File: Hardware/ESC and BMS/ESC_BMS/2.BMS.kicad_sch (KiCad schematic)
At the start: 39 parts, among them J301 SW IN, J302 SW OUT, Q301 SQJ141ELP, Q302 SQJ141ELP, Q303 FDV304P, Q304 PMV20XNEA, Q305 SQJ141ELP, U301 BQ2057W, U302 BQ2969

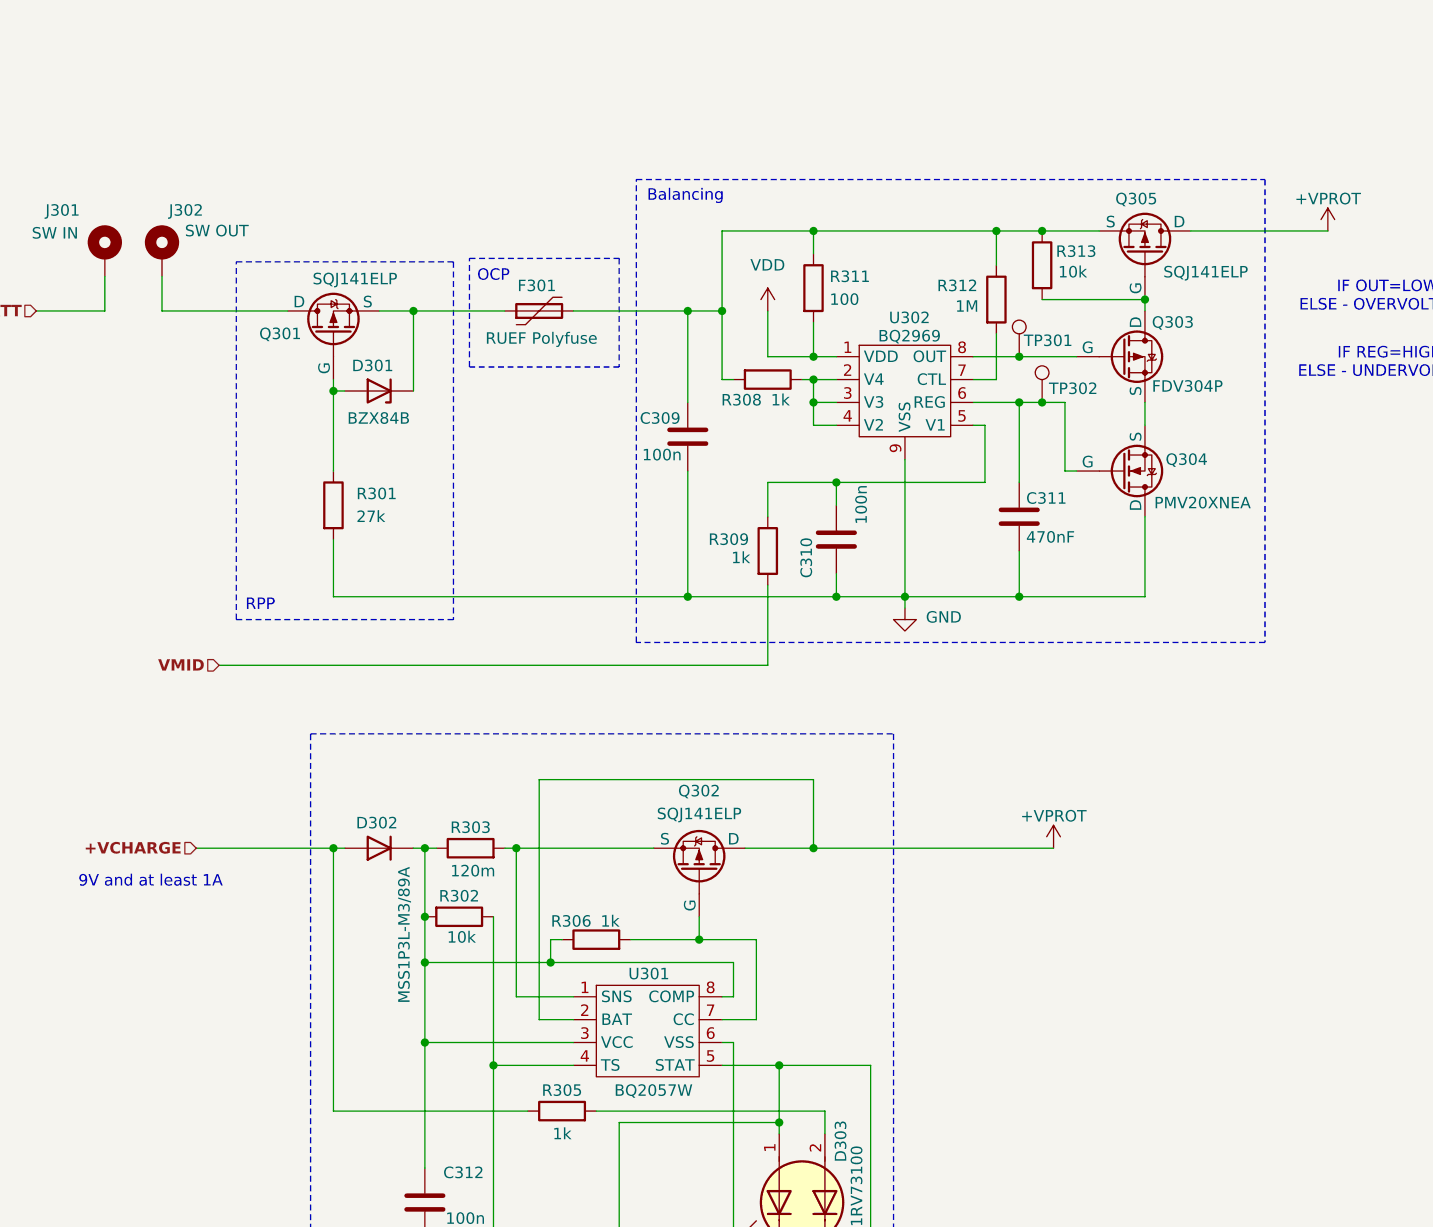
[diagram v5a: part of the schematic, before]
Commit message: Light rework of ESC/BMS layout
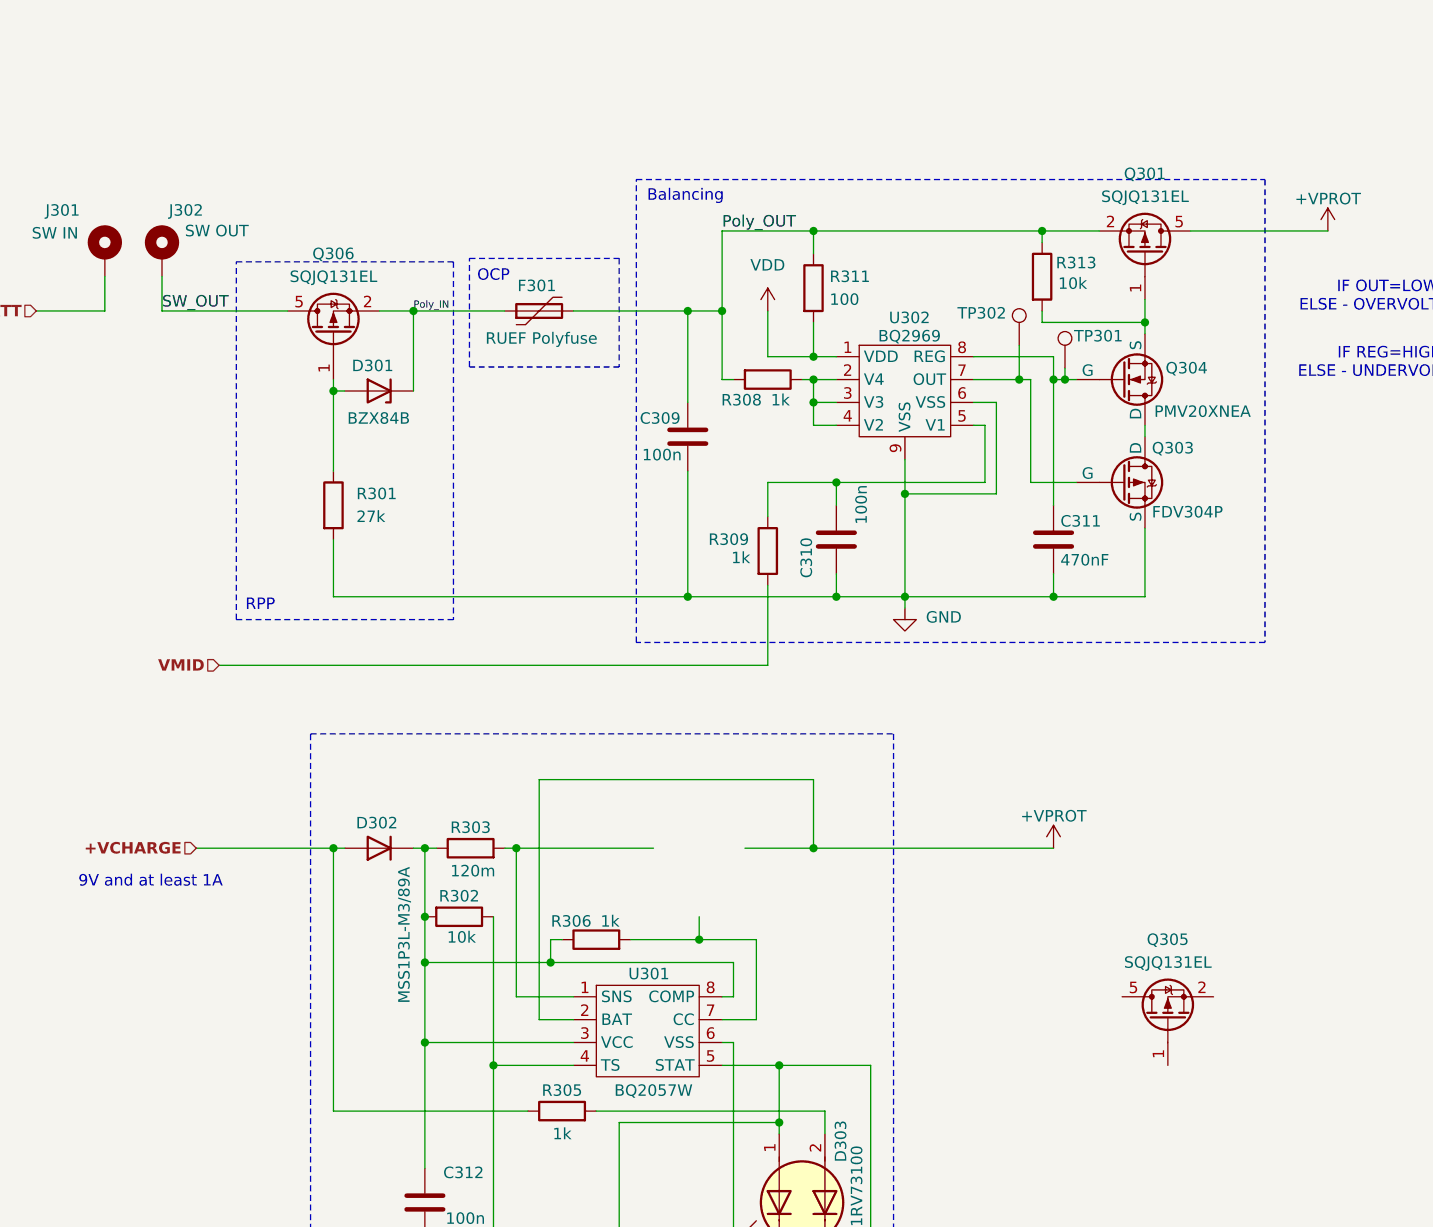
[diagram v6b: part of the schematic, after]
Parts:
- removed Q301, Q302, Q305: SQJ141ELP, Package_SO:PowerPAK_SO-8L_Single, symbol Simulation_SPICE:PMOS
- removed R312: 1M, Resistor_SMD:R_0805_2012Metric_Pad1.20x1.40mm_HandSolder, symbol Device:R
- added Q301, Q305, Q306: SQJQ131EL, Package_SO:PowerPAK_SO-8L_Single, symbol Transistor_FET:SQJQ131EL
- C302: footprint Capacitor_SMD:C_0805_2012Metric_Pad1.18x1.45mm_HandSolder -> Capacitor_SMD:C_0603_1608Metric_Pad1.08x0.95mm_HandSolder
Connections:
- net +VPROT: now also Q301.5 (D)
- net GND: now also Q303.3 (S), U302.6 (VSS); no longer Q304.1 (D)
- net at TP301.1, U302.8 (REG): now also C311.1, Q304.2 (G); no longer Q303.2 (G)
- net at R313.2: now also Q304.3 (S), Q301.1 (G); no longer Q303.1 (D)
- net Poly_OUT: now reaches C309.1, F301.2, R308.2, R311.1, R313.1
- net Poly_OUT: now also Q301.2 (S), Q301.3 (S), Q301.4 (S)
- net Poly_IN: now reaches D301.1 (K), F301.1
- net Poly_IN: now also Q306.2 (S), Q306.3 (S), Q306.4 (S)
- net at D301.2 (A), R301.1: now also Q306.1 (G)
- net SW_OUT: now reaches J302.1
- net SW_OUT: now also Q306.5 (D)
- net at U302.7 (OUT): now also Q303.2 (G), TP302.1
- new net: Q305.2 (S), Q305.3 (S), Q305.4 (S)
- new net: Q303.1 (D), Q304.1 (D)
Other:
- moved on the sheet: C311, Q303, Q304, R313, TP301, TP302

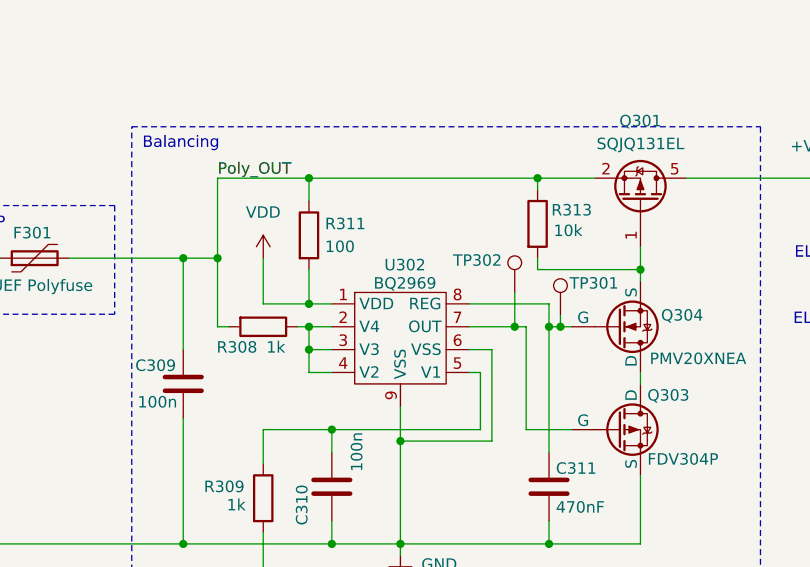
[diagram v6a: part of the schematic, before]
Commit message: ESC/BMS board done fully
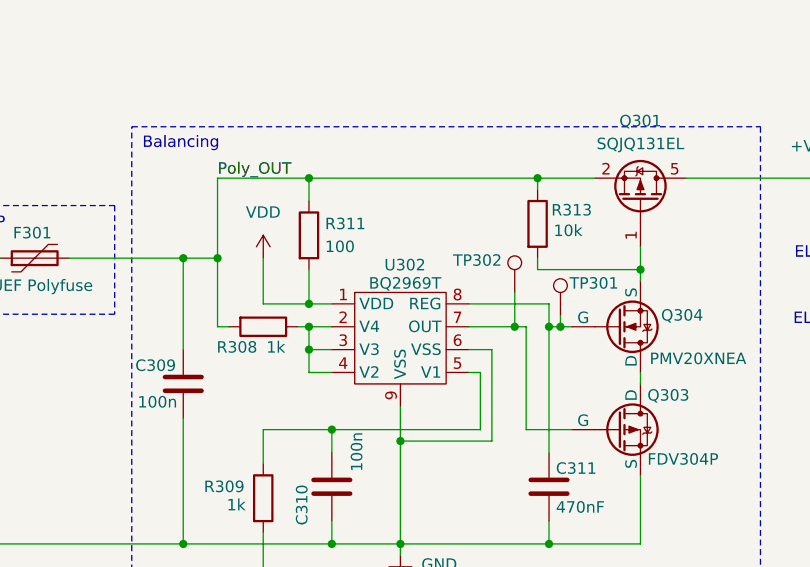
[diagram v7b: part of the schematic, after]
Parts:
- U302: value BQ2969 -> BQ2969T
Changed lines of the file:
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@@
 			)
 		)
-		(property "Value" "BQ2969"
+		(property "Value" "BQ2969T"
 			(at 226.568 98.044 0)
 			(effects

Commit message: ESC/BMS board done fully fully
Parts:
- U302: value BQ2969T -> BQ2969
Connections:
- net +VPROT: now also Q305.5 (D)
- net at Q305.1 (G): now also R306.2, U301.7 (CC)
- net at Q305.2 (S), Q305.3 (S), Q305.4 (S): now also R303.2, U301.1 (SNS)
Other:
- moved on the sheet: Q305
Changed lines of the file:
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@@
 	(symbol
 		(lib_id "Transistor_FET:SQJQ131EL")
-		(at 255.27 173.99 90)
-		(unit 1)
-		(exclude_from_sim no)
-		(in_bom yes)
-		(on_board yes)
-		(dnp no)
-		(fields_autoplaced yes)
+		(at 203.2 157.48 270)
+		(mirror x)
+		(unit 1)
+		(exclude_from_sim no)
+		(in_bom yes)
+		(on_board yes)
+		(dnp no)
 		(property "Reference" "Q305"
-			(at 255.27 165.1 90)
+			(at 203.2 148.59 90)
 			(effects
 				(font
@@
 		)
 		(property "Value" "SQJQ131EL"
-			(at 255.27 167.64 90)
+			(at 203.2 151.13 90)
 			(effects
 				(font
@@
 		)
 		(property "Footprint" "Package_SO:PowerPAK_SO-8L_Single"
-			(at 257.175 168.91 0)
+			(at 201.295 152.4 0)
 			(effects
 				(font
@@
 		)
 		(property "Datasheet" "https://docs.rs-online.com/afb1/A700000014240545.pdf"
-			(at 259.08 168.91 0)
+			(at 199.39 152.4 0)
 			(effects
 				(font
@@
 		)
 		(property "Description" "-232A Id, 340V Vds, P-Channel MOSFET, 1.4mOhm Ron, 82nC Qgd, -55 to 175 °C, LFPAK88"
-			(at 247.65 171.45 0)
+			(at 210.82 154.94 0)
 			(effects
 				(font
@@
 			)
 		)
-		(property "Value" "BQ2969T"
+		(property "Value" "BQ2969"
 			(at 226.568 98.044 0)
 			(effects
